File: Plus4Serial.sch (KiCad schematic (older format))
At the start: 17 parts, among them CN1 PLUS4_USERPORT, CN2 DB9_MALE, J1 JMP_CTS, U1 MC1489, U2 MC1488, U3 74HCT04

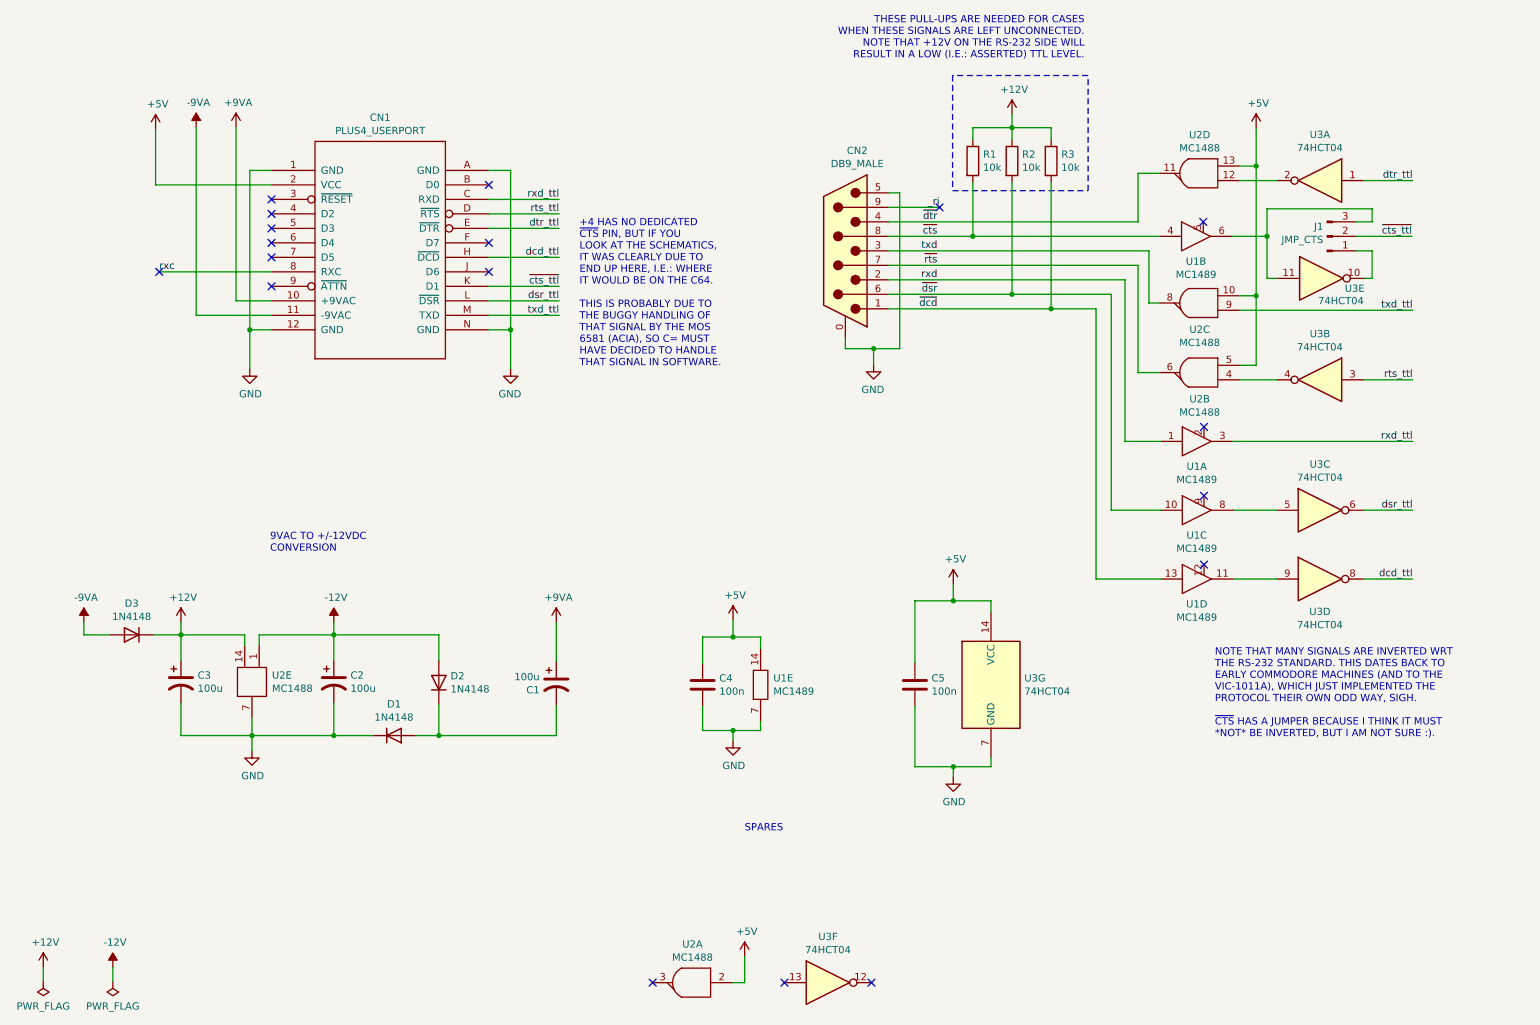
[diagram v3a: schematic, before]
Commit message: Switch to MAX238
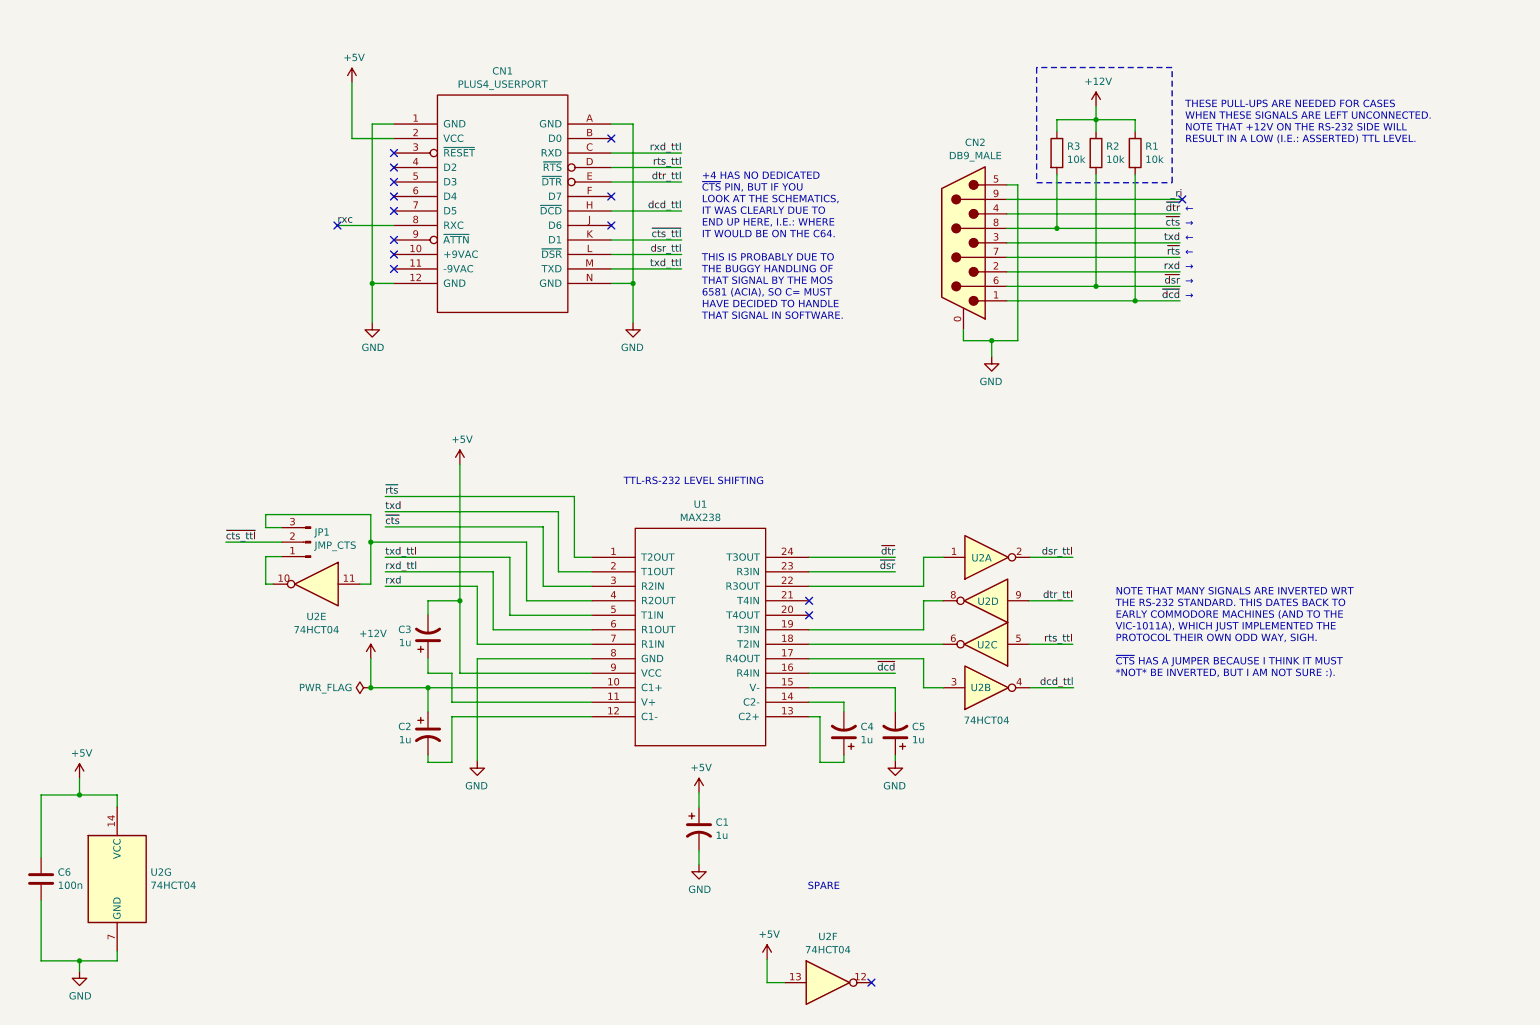
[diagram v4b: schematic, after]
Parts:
- removed C4: 100n, Capacitor_THT:C_Disc_D7.0mm_W2.5mm_P5.00mm, symbol Device:C
- removed D1, D2, D3: 1N4148, Diode_THT:D_DO-35_SOD27_P7.62mm_Horizontal, symbol Diode:1N4148
- removed U1: MC1489, Package_DIP:DIP-14_W7.62mm_Socket_LongPads, symbol mc1489:MC1489
- removed U2: MC1488, Package_DIP:DIP-14_W7.62mm_Socket_LongPads, symbol mc1488:MC1488
- added C4, C5: 1u, Capacitor_THT:CP_Radial_D5.0mm_P2.00mm, symbol Device:CP1
- added U1: MAX238, Package_DIP:DIP-24_W7.62mm_Socket_LongPads, symbol MAX238:MAX238
- C1, C2, C3: value 100u -> 1u; footprint Capacitor_THT:CP_Radial_D7.5mm_P2.50mm -> Capacitor_THT:CP_Radial_D5.0mm_P2.00mm; MouserPN (none) -> 710-860010672005
- R1: renamed from R3; footprint Resistor_THT:R_Axial_DIN0207_L6.3mm_D2.5mm_P10.16mm_Horizontal -> Resistor_THT:R_Axial_DIN0207_L6.3mm_D2.5mm_P5.08mm_Vertical
- R2: footprint Resistor_THT:R_Axial_DIN0207_L6.3mm_D2.5mm_P10.16mm_Horizontal -> Resistor_THT:R_Axial_DIN0207_L6.3mm_D2.5mm_P5.08mm_Vertical
- R3: renamed from R1; footprint Resistor_THT:R_Axial_DIN0207_L6.3mm_D2.5mm_P10.16mm_Horizontal -> Resistor_THT:R_Axial_DIN0207_L6.3mm_D2.5mm_P5.08mm_Vertical
- U2: renamed from U3; MouserPN (none) -> 595-SN74HCT04NE4
- renumbered C5 to C6, J1 to JP1
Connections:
- net -12V is gone; now on net +12V: C2.1
- net +12V: now also U1.10 (C1+); no longer C3.1
- net +5V: now also C1.1, C3.2, U2.13, U1.9 (VCC)
- net GND: now also C1.2, C5.1, U1.8 (GND); no longer C2.2, C3.2
- net dcd_ttl: now also U2.4; no longer U2.8
- net dsr_ttl: now also U2.2; no longer U2.6
- net dtr_ttl: now also U2.9; no longer U2.1
- net rts_ttl: now also U2.5; no longer U2.3
- net rxd: now also U1.7 (R1IN)
- net rxd_ttl: now also U1.6 (R1OUT)
- net txd: now also U1.2 (T1OUT)
- net txd_ttl: now also U1.5 (T1IN)
- net ~cts: now also U1.3 (R2IN)
- net ~dcd: now also U1.16 (R4IN)
- net ~dsr: now also U1.23 (R3IN)
- net ~dtr: now also U1.24 (T3OUT)
- net ~rts: now also U1.1 (T2OUT)
- net at JP1.3 (Pin_3), U2.11: now also U1.4 (R2OUT)
- net +9VA: no longer names the net of CN1.10 (+9VAC)
- net +9VA: no longer C1.1
- net -9VA: no longer names the net of CN1.11 (-9VAC)
- new net: U1.22 (R3OUT), U2.1
- new net: U1.17 (R4OUT), U2.3
- new net: U1.18 (T2IN), U2.6
- new net: U1.19 (T3IN), U2.8
- new net: C4.1, U1.13 (C2+)
- new net: C4.2, U1.14 (C2-)
- new net: C5.2, U1.15 (V-)
- new net: C3.1, U1.11 (V+)
- new net: C2.2, U1.12 (C1-)
- no-connect marks 18 -> 16
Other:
- note added: "SPARE"
- note added: "TTL-RS-232 LEVEL SHIFTING"
- note added: "←"
- note added: "→"
- note removed: "9VAC TO +/-12VDC\nCONVERSION"
- note removed: "SPARES"
- moved on the sheet: C6, CN1, CN2, JP1, R1, R2, R3, U2A, U2B, U2C, U2D, U2E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

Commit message: Take +12V from correct pin
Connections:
- net +12V: now also C3.1, U1.11 (V+); no longer C2.1, U1.10 (C1+)
- new net: C2.1, U1.10 (C1+)
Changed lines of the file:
@@
 	6085 5220 6875 5220
 Wire Wire Line
-	3455 5420 3060 5420
+	3455 5320 3060 5320
 Wire Wire Line
-	3060 5420 3060 5220
-Connection ~ 3455 5420
+	3060 5320 3060 5120
 $Comp
 L power:+12V #PWR0101
 U 1 1 636B5308
-P 3060 5220
-F 0 "#PWR0101" H 3060 5070 50  0001 C CNN
-F 1 "+12V" H 3075 5393 50  0000 C CNN
-F 2 "" H 3060 5220 50  0001 C CNN
-F 3 "" H 3060 5220 50  0001 C CNN
-	1    3060 5220
+P 3060 5120
+F 0 "#PWR0101" H 3060 4970 50  0001 C CNN
+F 1 "+12V" H 3075 5293 50  0000 C CNN
+F 2 "" H 3060 5120 50  0001 C CNN
+F 3 "" H 3060 5120 50  0001 C CNN
+	1    3060 5120
 	1    0    0    -1
 $EndComp
@@
 L power:PWR_FLAG #FLG0101
 U 1 1 636BC8D8
-P 3060 5420
-F 0 "#FLG0101" H 3060 5495 50  0001 C CNN
-F 1 "PWR_FLAG" V 3060 5547 50  0000 L CNN
-F 2 "" H 3060 5420 50  0001 C CNN
-F 3 "~" H 3060 5420 50  0001 C CNN
-	1    3060 5420
+P 3060 5320
+F 0 "#FLG0101" H 3060 5395 50  0001 C CNN
+F 1 "PWR_FLAG" V 3060 5447 50  0000 L CNN
+F 2 "" H 3060 5320 50  0001 C CNN
+F 3 "~" H 3060 5320 50  0001 C CNN
+	1    3060 5320
 	0    -1   -1   0
 $EndComp
-Connection ~ 3060 5420
+Connection ~ 3060 5320
 Wire Wire Line
 	5915 7455 5795 7455
@@
 	1    0    0    1
 $EndComp
+Connection ~ 3455 5320
 $EndSCHEMATC

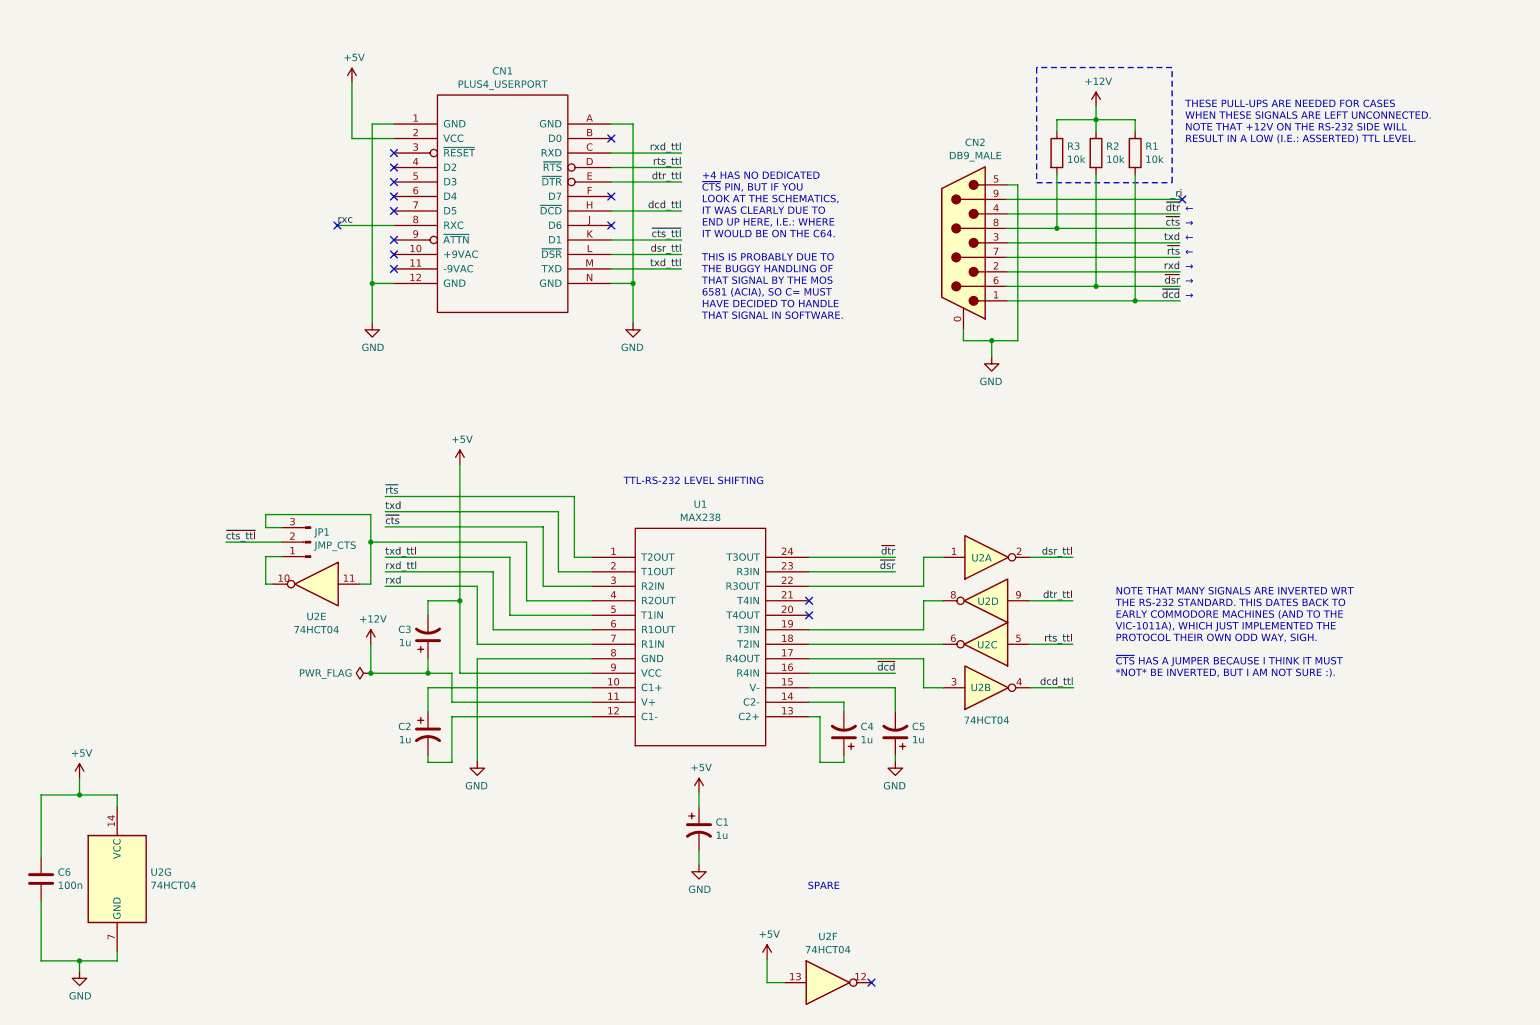
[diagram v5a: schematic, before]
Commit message: Remove CTS/_CTS jumper Now we know for certain that CTS is active-high on the User Port
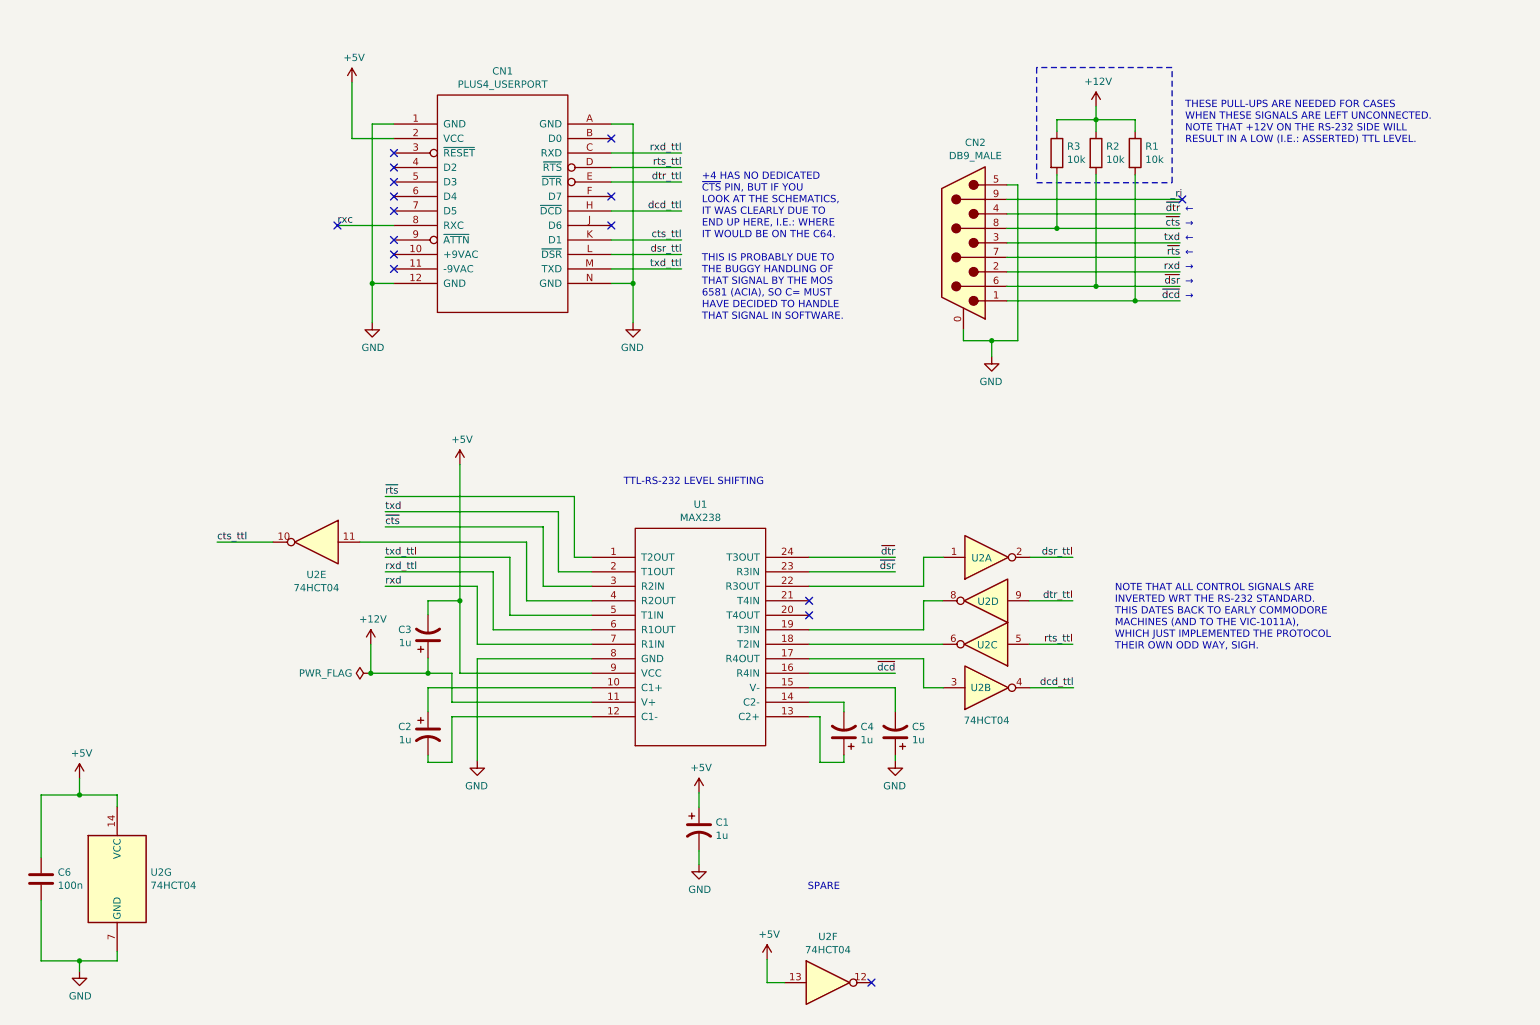
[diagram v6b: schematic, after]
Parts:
- removed JP1: JMP_CTS, Connector_PinHeader_2.54mm:PinHeader_1x03_P2.54mm_Vertical, symbol Connector:Conn_01x03_Male
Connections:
- net ~cts_ttl is gone; now on net cts_ttl: CN1.K (D1)
- net cts_ttl: now reaches U2.10
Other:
- note added: "NOTE THAT ALL CONTROL SIGNALS ARE\nINVERTED WRT THE RS-232 STANDARD.\nTHIS DATES BACK TO EARLY COMMODORE\nMACHINES (AND TO THE VIC-1011A),\nWHICH JUST IMPLEMENTED THE PROTOCOL\nTHEIR OWN ODD WAY, SIGH."
- note removed: "NOTE THAT MANY SIGNALS ARE INVERTED WRT\nTHE RS-232 STANDARD. THIS DATES BACK TO\nEARLY COMMODORE MACHINES (AND TO THE\nVIC-1011A), WHICH JUST IMPLEMENTED THE\nPROTOCOL THEIR OWN ODD WAY, SIGH.\n\n~CTS~ HAS A JUMPER BECAUSE I THINK IT MUST\n*NOT* BE INVERTED, BUT I AM NOT SURE :)."
- moved on the sheet: U2E
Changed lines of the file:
@@
 Sheet 1 1
 Title "Plus4Serial"
-Date "2022-09-28"
-Rev "1git"
+Date "2022-11-02"
+Rev "2git"
 Comp "SukkoPera"
 Comment1 "Thanks a lot to Levente Hársfalvi (TLC)!"
@@
 NoConn ~ 8660 2050
 Text Label 5205 2330 2    50   ~ 0
-~cts_ttl
+cts_ttl
 Wire Wire Line
 	4720 2330 5205 2330
@@
 Wire Wire Line
 	1050 6160 1310 6160
-Text Notes 8200 5355 0    50   ~ 0
-NOTE THAT MANY SIGNALS ARE INVERTED WRT\nTHE RS-232 STANDARD. THIS DATES BACK TO\nEARLY COMMODORE MACHINES (AND TO THE\nVIC-1011A), WHICH JUST IMPLEMENTED THE\nPROTOCOL THEIR OWN ODD WAY, SIGH.\n\n~CTS~ HAS A JUMPER BECAUSE I THINK IT MUST\n*NOT* BE INVERTED, BUT I AM NOT SURE :).
+Text Notes 8195 5165 0    50   ~ 0
+NOTE THAT ALL CONTROL SIGNALS ARE\nINVERTED WRT THE RS-232 STANDARD.\nTHIS DATES BACK TO EARLY COMMODORE\nMACHINES (AND TO THE VIC-1011A),\nWHICH JUST IMPLEMENTED THE PROTOCOL\nTHEIR OWN ODD WAY, SIGH.
 $Comp
 L Device:R R3
@@
 Wire Wire Line
 	8065 1500 8065 1410
-Text Label 2060 4415 0    50   ~ 0
-~cts_ttl
+Text Label 2000 4415 0    50   ~ 0
+cts_ttl
 Wire Wire Line
 	7450 2250 7795 2250
@@
 Text Notes 8680 1670 0    50   ~ 0
 THESE PULL-UPS ARE NEEDED FOR CASES\nWHEN THESE SIGNALS ARE LEFT UNCONNECTED.\nNOTE THAT +12V ON THE RS-232 SIDE WILL\nRESULT IN A LOW (I.E.: ASSERTED) TTL LEVEL.
-$Comp
-L Connector:Conn_01x03_Male JP1
-U 1 1 634CF0C8
-P 2645 4415
-F 0 "JP1" H 2618 4347 50  0000 R CNN
-F 1 "JMP_CTS" H 2618 4438 50  0000 R CNN
-F 2 "Connector_PinHeader_2.54mm:PinHeader_1x03_P2.54mm_Vertical" H 2645 4415 50  0001 C CNN
-F 3 "~" H 2645 4415 50  0001 C CNN
-	1    2645 4415
-	-1   0    0    1
-$EndComp
-Wire Wire Line
-	2445 4415 2060 4415
-Wire Wire Line
-	2335 4705 2335 4515
-Wire Wire Line
-	2335 4515 2445 4515
-Wire Wire Line
-	2335 4225 2335 4315
-Wire Wire Line
-	2335 4315 2445 4315
+Wire Wire Line
+	2385 4415 2000 4415
 $Comp
 L 74xx:74HCT04 U2
 U 5 1 6333E12B
-P 2685 4705
-F 0 "U2" H 2685 4480 50  0000 C CNN
-F 1 "74HCT04" H 2685 4389 50  0000 C CNN
-F 2 "Package_DIP:DIP-14_W7.62mm_Socket_LongPads" H 2685 4705 50  0001 C CNN
-F 3 "https://assets.nexperia.com/documents/data-sheet/74HC_HCT04.pdf" H 2685 4705 50  0001 C CNN
-F 4 "595-SN74HCT04NE4" H 2685 4705 50  0001 C CNN "MouserPN"
-	5    2685 4705
+P 2685 4415
+F 0 "U2" H 2685 4190 50  0000 C CNN
+F 1 "74HCT04" H 2685 4099 50  0000 C CNN
+F 2 "Package_DIP:DIP-14_W7.62mm_Socket_LongPads" H 2685 4415 50  0001 C CNN
+F 3 "https://assets.nexperia.com/documents/data-sheet/74HC_HCT04.pdf" H 2685 4415 50  0001 C CNN
+F 4 "595-SN74HCT04NE4" H 2685 4415 50  0001 C CNN "MouserPN"
+	5    2685 4415
 	-1   0    0    -1
 $EndComp
-Wire Wire Line
-	2385 4705 2335 4705
-Connection ~ 3060 4415
-Wire Wire Line
-	3060 4225 2335 4225
-Wire Wire Line
-	3060 4415 3060 4225
-Wire Wire Line
-	3060 4705 2985 4705
-Wire Wire Line
-	3060 4415 3060 4705
 Wire Wire Line
 	7795 2250 7795 1880
@@
 $EndComp
 Wire Wire Line
-	3060 4415 4135 4415
-Wire Wire Line
 	7605 5120 7905 5120
 Wire Wire Line
@@
 $EndComp
 Connection ~ 3455 5320
+Wire Wire Line
+	2985 4415 4135 4415
 $EndSCHEMATC
